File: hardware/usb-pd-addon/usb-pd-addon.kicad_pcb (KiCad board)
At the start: 4 copper layers, 48 x 40 mm, 75 parts, among them J1 TARGET, J2 SNOOP, J3 Conn_02x10_Odd_Even, J4 Conn_02x10_Odd_Even, J5 ADCB, J6 ADCA, J7 D+/D- ISOLATION, J8 SBU1/SBU2 ISOLATION, J9 Conn_02x03_Odd_Even, U1 SN74AVC1T45DCKR, U10 FUSB302B, U11 AP2127K-ADJ, U2 NC7SB3157P6X, U3 SN74AVC1T45DCKR, U4 NC7SB3157P6X, U5 SN74AVC1T45DCKR, U6 NC7SB3157P6X, U7 SN74AVC1T45DCKR, U8 NC7SB3157P6X, U9 AP2171W

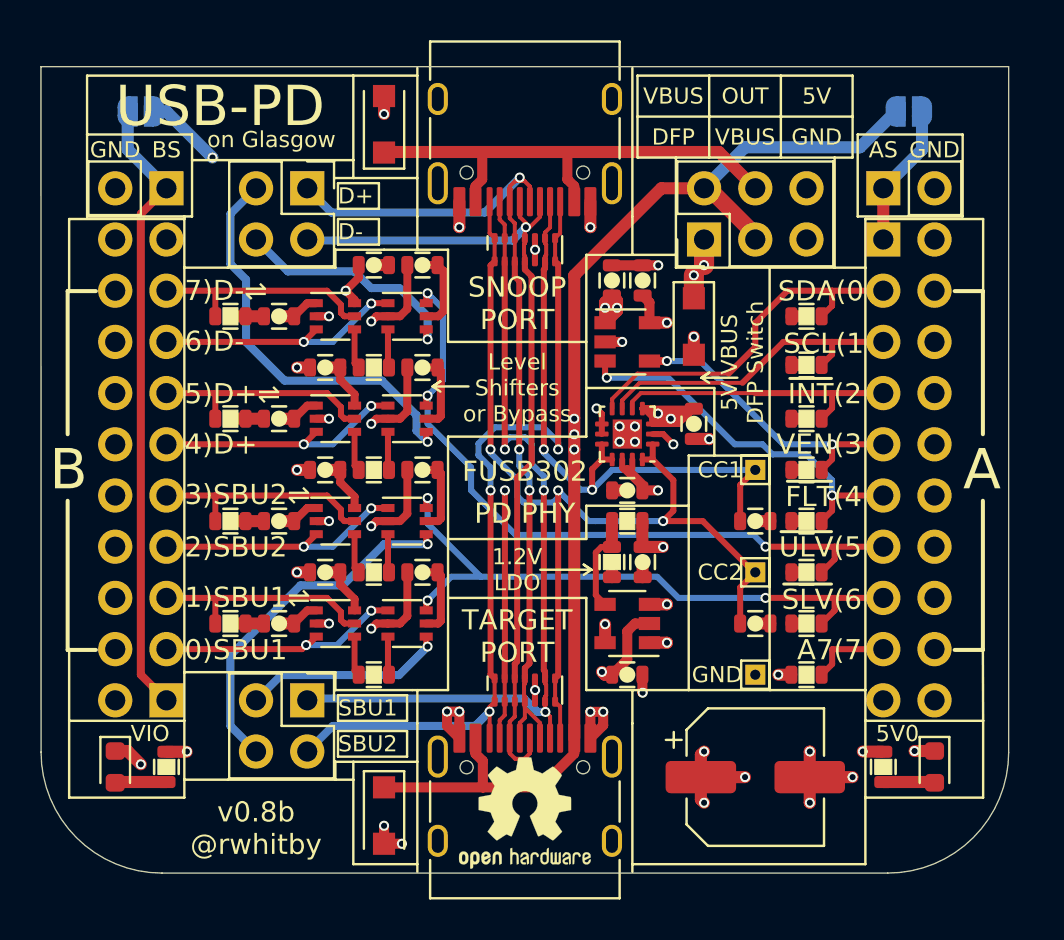
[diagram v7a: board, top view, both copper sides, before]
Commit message: v0.8c: Added 1.2V test point and more front silk improvements.
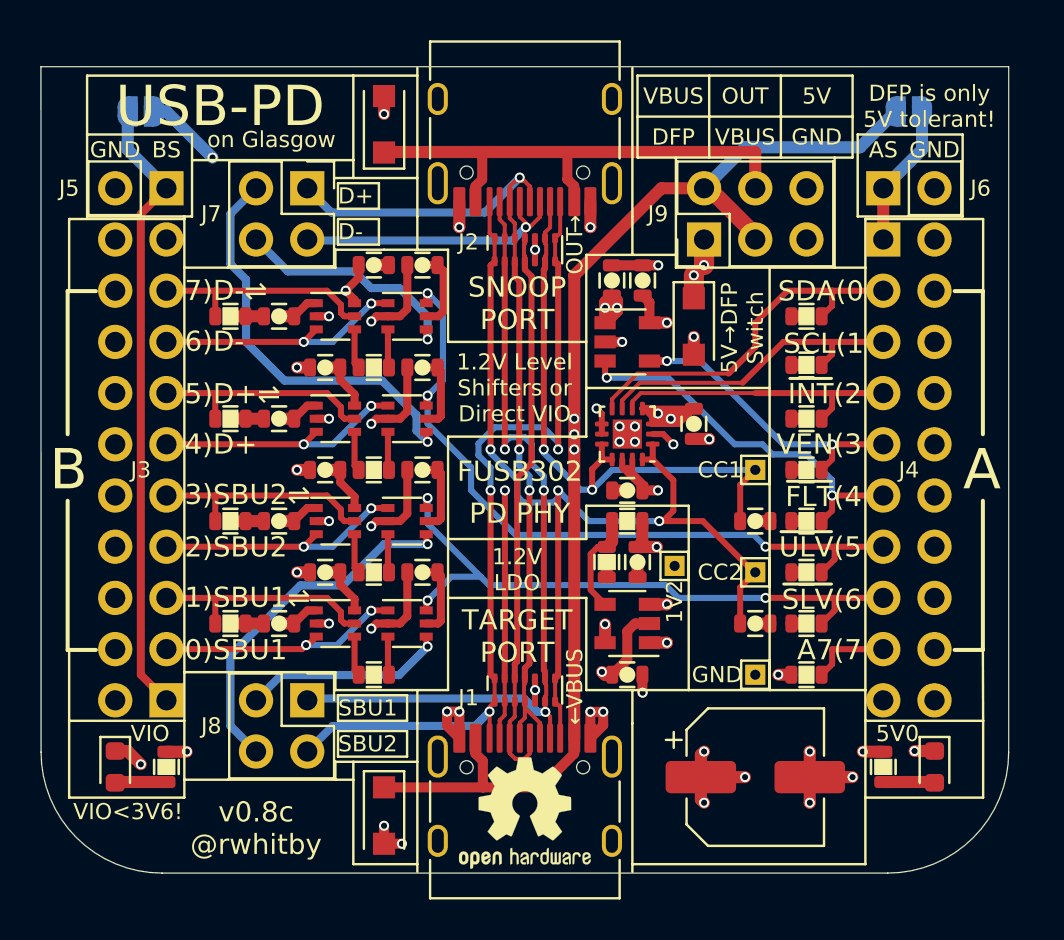
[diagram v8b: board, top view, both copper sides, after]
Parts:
- added TP4: TestPoint, TestPoint:TestPoint_THTPad_1.0x1.0mm_Drill0.5mm, F.Cu at (63.3, 56.8)
- moved C17 0.25 mm to (61.5, 56.6)
- moved R10 0.25 mm to (59.9, 56.6)
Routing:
- net /1.2V: track 66.3 -> 68.6 mm
- net /VBUS_OUT: track 24.4 -> 25.4 mm
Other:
- board text added: "1.2V Level Shifters or Direct VIO"
- board text added: "1V2"
- board text added: "5V→DFP Switch"
- board text added: "DFP is only 5V tolerant!"
- board text added: "J1"
- board text added: "J2"
- board text added: "J3"
- board text added: "J4"
- board text added: "J5"
- board text added: "J6"
- board text added: "J7"
- board text added: "J8"
- board text added: "J9"
- board text added: "VIO<3V6!"
- board text added: "v0.8c @rwhitby"
- board text added: "←"
- board text added: "→"
- board text removed: "5V VBUS DFP Switch"
- board text removed: "Level Shifters or Bypass"
- board text removed: "v0.8b @rwhitby"
